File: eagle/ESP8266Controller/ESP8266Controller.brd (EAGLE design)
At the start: 61 x 48.3 mm, 22 parts, among them J1 POWER_JACKPTH

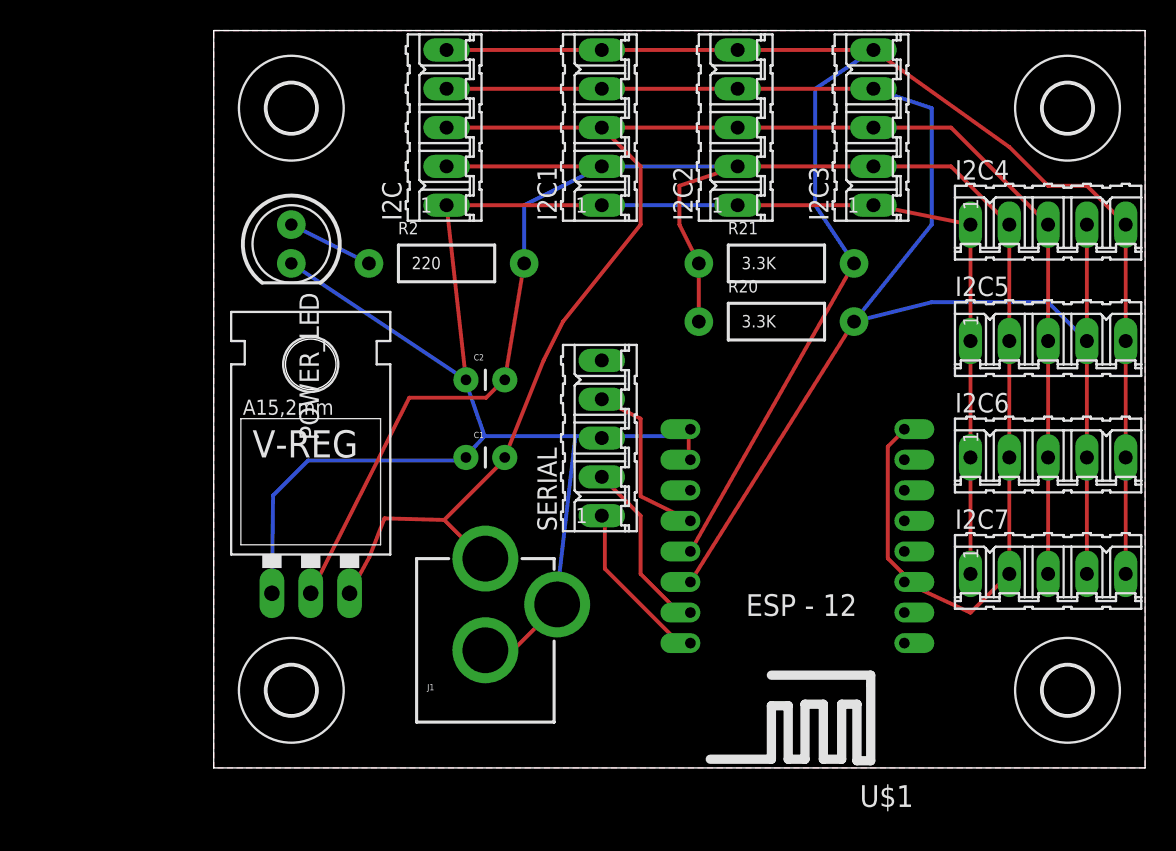
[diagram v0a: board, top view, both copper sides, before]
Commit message: 1.  More additions to the API 2.  Rename device.moduleIndex to device.port 3.  Begin work on new InputModule 4.  Module:  remove unused functions: 	virtual byte getDeviceCount(void) const = 0; 	virtual short getDeviceID(byte index) const = 0;
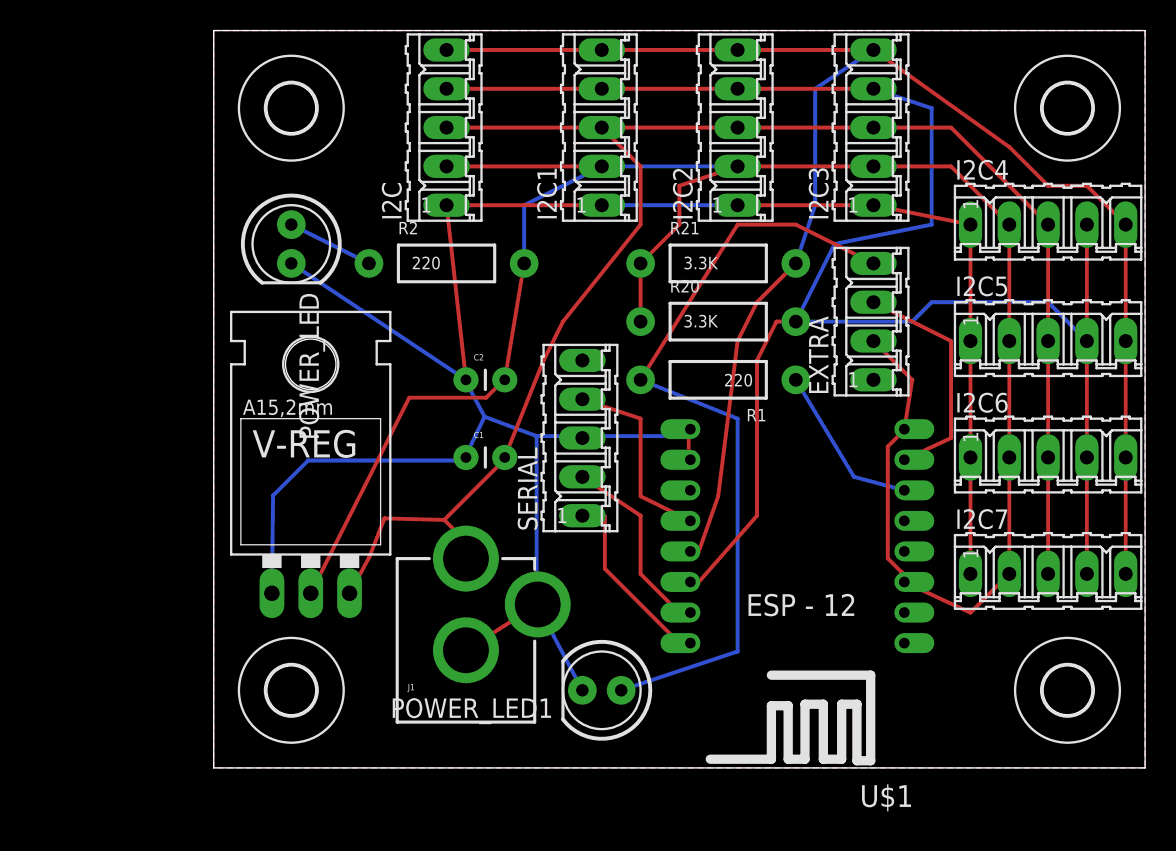
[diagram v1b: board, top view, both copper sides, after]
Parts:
- added EXTRA: PIN0, con-amp-quick:04P
- added POWER_LED1: 3.3, SparkFun-LED:LED5MM
- added R1: 220, SparkFun-Resistors:AXIAL-0.4
- moved R20 3.81 mm to (33.0, 29.2)
- moved R21 3.81 mm to (33.0, 33.0)
- moved J1 1.27 mm to (16.5, 0.00)
- moved SERIAL 1.27 mm to (24.1, 21.6)
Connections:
- removed net N$34: U$1.GPIO14
- removed net N$35: U$1.GPIO12
- removed net N$36: U$1.GPIO2
- new net N$1: EXTRA.4, POWER_LED1.A, R1.P$2
- new net N$2: R1.P$1, U$1.GPIO12
- new net N$3: EXTRA.3, U$1.GPIO13
- net +3V3: now also EXTRA.2
- net GND: now also EXTRA.1, POWER_LED1.K
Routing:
- net N$1: track 0.00 -> 51.6 mm
- net N$3: track 0.00 -> 15.4 mm
- net N$2: track 0.00 -> 10.8 mm
- net N$8: track 107.1 -> 115.8 mm
- net +3V3: track 132.0 -> 139.6 mm
- net GND: track 141.5 -> 147.4 mm
- net N$4: track 11.2 -> 12.5 mm
- net N$6: track 109.9 -> 108.7 mm
- net N$19: track 11.6 -> 12.7 mm
- net N$11: track 11.7 -> 12.7 mm
- net VCC: track 108.9 -> 109.8 mm

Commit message: 1.  Cleanup continues.  BlockController and the corresponding controller are deprecated along with SignalController and it's controller board.  These are replaced by the InputModule and OutputModule respectively 2.  TurnoutHandler moved to the MultiModuleController project folder 3.  Module moved to the MultiModuleController project folder 4.  More database cleanup work completed.
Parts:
- removed POWER_LED1: 3.3, SparkFun-LED:LED5MM
- EXTRA: value PIN0 -> (none)
- I2C, I2C1, I2C2, I2C3, I2C4, I2C5, I2C6, I2C7: value PIN1 -> (none)
- turned R1 to 0 degrees
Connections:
- net N$6 renamed SDA
- net N$8 renamed SCL
- net GND: no longer POWER_LED1.K
- net N$1: no longer POWER_LED1.A
- net N$2: now also U$1.GPIO2; no longer U$1.GPIO12
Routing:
- net N$1: track 51.6 -> 10.2 mm
- net VCC: track 109.8 -> 106.9 mm
- net N$2: track 10.8 -> 9.73 mm
- net N$19: track 12.7 -> 12.0 mm
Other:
- board text added: "+"
- board text added: "-"
- board text added: "Layout Ctrl ESP 8266 Controller Version 2.1"
- board text added: "PIN0"
- board text added: "PWR"

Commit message: 1.  Add jitter-detection to BlockDevice 2.  Add flashing pins to  ModuleData 3.  Move flashing pin code from PanelOutputDevice to OutputModule.  This insures pins blink at the same rate and same state. 4.  Fix flashing code for PanelInputDevice/OutputModule 5.  Remove unused code from PanelInputDevice 6.  fix jitter-detection code in TurnoutDevice 7.  New checkbox on StatusDialog allows enabling/disabling of server heartbeat messages 8.  Remove one of the I2C connections from the LCS Controller to make room for labels for the I2C pins 9.  Up build version to 19
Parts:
- removed I2C7: (no value), con-amp-quick:05P
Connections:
- net +3V3: no longer I2C7.2
- net GND: no longer I2C7.1
- net SCL: no longer I2C7.4
- net SDA: no longer I2C7.5
- net VCC: no longer I2C7.3
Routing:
- net VCC: track 106.9 -> 99.3 mm
- net SDA: track 108.7 -> 101.1 mm
- net SCL: track 115.8 -> 108.2 mm
- net GND: track 147.9 -> 140.3 mm
- net +3V3: track 139.6 -> 134.5 mm
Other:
- board text added: "+3.3v"
- board text added: ".1uF"
- board text added: "10uF"
- board text added: "GND"
- board text added: "LCS Controller Version 2.2"
- board text added: "SCA"
- board text added: "SCL"
- board text added: "VCC"
- board text removed: "Layout Ctrl ESP 8266 Controller Version 2.1"
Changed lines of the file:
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@@
 <wire x1="60.96" y1="48.26" x2="0" y2="48.26" width="0" layer="20"/>
 <wire x1="0" y1="48.26" x2="0" y2="0" width="0" layer="20"/>
-<text x="29.21" y="1.27" size="1.27" layer="21" rot="R90">Layout Ctrl
-ESP 8266
+<text x="27.94" y="1.27" size="1.27" layer="21" rot="R90">LCS
 Controller
-Version 2.1</text>
+Version 2.2</text>
 <text x="46.99" y="24.13" size="1.27" layer="21" rot="R90">PIN0</text>
 <text x="6.35" y="38.1" size="1.778" layer="21" rot="R315">PWR</text>
@@
 <text x="19.05" y="17.78" size="1.778" layer="21">+</text>
 <text x="20.32" y="35.56" size="1.778" layer="21" rot="R90">PIN0</text>
-<text x="48.26" y="15.24" size="1.778" layer="21">PIN0</text>
+<text x="49.53" y="13.97" size="1.27" layer="21" rot="R90">GND</text>
+<text x="52.07" y="12.7" size="1.27" layer="21" rot="R90">+3.3v</text>
+<text x="54.61" y="13.97" size="1.27" layer="21" rot="R90">VCC</text>
+<text x="57.15" y="13.97" size="1.27" layer="21" rot="R90">SCL</text>
+<text x="59.69" y="13.97" size="1.27" layer="21" rot="R90">SCA</text>
+<text x="19.05" y="29.21" size="1.27" layer="21" rot="R180">10uF</text>
+<text x="19.05" y="19.05" size="1.27" layer="21" rot="R180">.1uF</text>
 </plain>
 <attributes>
@@
 <attribute name="OC_FARNELL" value="unknown" x="54.61" y="20.32" size="1.778" layer="27" display="off"/>
 </element>
-<element name="I2C7" library="con-amp-quick" package="05P" value="" x="54.61" y="12.7">
-<attribute name="OC_NEWARK" value="unknown" x="54.61" y="12.7" size="1.778" layer="27" display="off"/>
-<attribute name="MPN" value="" x="54.61" y="12.7" size="1.778" layer="27" display="off"/>
-<attribute name="MF" value="" x="54.61" y="12.7" size="1.778" layer="27" display="off"/>
-<attribute name="OC_FARNELL" value="unknown" x="54.61" y="12.7" size="1.778" layer="27" display="off"/>
-</element>
 <element name="R1" library="SparkFun-Resistors" package="AXIAL-0.4" value="220" x="33.02" y="25.4"/>
 <element name="EXTRA" library="con-amp-quick" package="04P" value="" x="43.18" y="29.21" rot="R90">
@@
 <contactref element="I2C5" pad="1"/>
 <contactref element="I2C6" pad="1"/>
-<contactref element="I2C7" pad="1"/>
 <wire x1="5.08" y1="33.02" x2="16.51" y2="25.4" width="0.254" layer="16"/>
 <wire x1="15.24" y1="36.83" x2="25.4" y2="36.83" width="0.254" layer="1"/>
@@
 </polygon>
 <wire x1="49.53" y1="20.32" x2="49.53" y2="27.94" width="0.254" layer="1"/>
-<wire x1="49.53" y1="12.7" x2="49.53" y2="20.32" width="0.254" layer="1"/>
 <wire x1="49.53" y1="27.94" x2="49.53" y2="35.56" width="0.254" layer="1"/>
 <wire x1="43.18" y1="36.83" x2="49.53" y2="35.56" width="0.254" layer="1"/>
@@
 <wire x1="18.9738" y1="25.3746" x2="17.8308" y2="24.2316" width="0.254" layer="1"/>
 <wire x1="18.9738" y1="25.3746" x2="19.05" y2="25.4" width="0.254" layer="1"/>
-<wire x1="45.0342" y1="12.8016" x2="45.0342" y2="12.3444" width="0.254" layer="1"/>
-<wire x1="44.1198" y1="13.716" x2="45.0342" y2="12.8016" width="0.254" layer="1"/>
-<wire x1="44.1198" y1="21.0312" x2="44.1198" y2="13.716" width="0.254" layer="1"/>
-<wire x1="45.0342" y1="21.9456" x2="44.1198" y2="21.0312" width="0.254" layer="1"/>
-<wire x1="45.0342" y1="12.3444" x2="45.2" y2="12.17" width="0.254" layer="1"/>
-<wire x1="45.0342" y1="21.9456" x2="45.2" y2="22.17" width="0.254" layer="1"/>
 <contactref element="I2C1" pad="2"/>
 <contactref element="I2C2" pad="2"/>
@@
 <contactref element="I2C5" pad="2"/>
 <contactref element="I2C6" pad="2"/>
-<contactref element="I2C7" pad="2"/>
 <wire x1="34.29" y1="39.37" x2="43.18" y2="39.37" width="0.254" layer="1"/>
 <wire x1="25.4" y1="39.37" x2="15.24" y2="39.37" width="0.254" layer="1"/>
 <wire x1="19.05" y1="25.4" x2="20.32" y2="33.02" width="0.254" layer="1"/>
-<wire x1="45.2" y1="12.17" x2="49.53" y2="10.16" width="0.254" layer="1"/>
-<wire x1="49.53" y1="10.16" x2="52.07" y2="12.7" width="0.254" layer="1"/>
 <wire x1="52.07" y1="20.32" x2="52.07" y2="27.94" width="0.254" layer="1"/>
-<wire x1="52.07" y1="12.7" x2="52.07" y2="20.32" width="0.254" layer="1"/>
 <wire x1="52.07" y1="27.94" x2="52.07" y2="35.56" width="0.254" layer="1"/>
 <wire x1="43.18" y1="39.37" x2="48.26" y2="39.37" width="0.254" layer="1"/>
@@
 <wire x1="43.18" y1="27.94" x2="45.72" y2="25.4" width="0.254" layer="1"/>
 <wire x1="45.72" y1="25.4" x2="45.2" y2="22.17" width="0.254" layer="1"/>
+<wire x1="45.2" y1="22.17" x2="43.18" y2="20.32" width="0.254" layer="1"/>
+<wire x1="43.18" y1="20.32" x2="43.18" y2="12.7" width="0.254" layer="1"/>
+<wire x1="43.18" y1="12.7" x2="45.2" y2="12.17" width="0.254" layer="1"/>
+<wire x1="52.07" y1="27.94" x2="50.8" y2="25.4" width="0.254" layer="16"/>
+<wire x1="50.8" y1="25.4" x2="45.2" y2="22.17" width="0.254" layer="16"/>
 </signal>
 <signal name="VCC">
@@
 <contactref element="I2C5" pad="3"/>
 <contactref element="I2C6" pad="3"/>
-<contactref element="I2C7" pad="3"/>
 <wire x1="43.18" y1="41.91" x2="34.29" y2="41.91" width="0.254" layer="1"/>
 <wire x1="34.29" y1="41.91" x2="25.4" y2="41.91" width="0.254" layer="1"/>
@@
 <wire x1="27.94" y1="39.37" x2="25.4" y2="41.91" width="0.254" layer="1"/>
 <wire x1="54.61" y1="20.32" x2="54.61" y2="27.94" width="0.254" layer="1"/>
-<wire x1="54.61" y1="12.7" x2="54.61" y2="20.32" width="0.254" layer="1"/>
 <wire x1="54.61" y1="27.94" x2="54.61" y2="35.56" width="0.254" layer="1"/>
 <wire x1="43.18" y1="41.91" x2="48.26" y2="41.91" width="0.254" layer="1"/>
@@
 <contactref element="I2C5" pad="5"/>
 <contactref element="I2C6" pad="5"/>
-<contactref element="I2C7" pad="5"/>
-<wire x1="59.69" y1="12.7" x2="59.69" y2="20.32" width="0.254" layer="1"/>
 <wire x1="43.18" y1="46.99" x2="34.29" y2="46.99" width="0.254" layer="1"/>
 <wire x1="34.29" y1="46.99" x2="25.4" y2="46.99" width="0.254" layer="1"/>
@@
 <contactref element="I2C5" pad="4"/>
 <contactref element="I2C6" pad="4"/>
-<contactref element="I2C7" pad="4"/>
 <wire x1="15.24" y1="44.45" x2="25.4" y2="44.45" width="0.254" layer="1"/>
 <wire x1="25.4" y1="44.45" x2="34.29" y2="44.45" width="0.254" layer="1"/>
@@
 <wire x1="40.64" y1="34.29" x2="38.1" y2="29.21" width="0.254" layer="16"/>
 <wire x1="57.15" y1="20.32" x2="57.15" y2="27.94" width="0.254" layer="1"/>
-<wire x1="57.15" y1="12.7" x2="57.15" y2="20.32" width="0.254" layer="1"/>
 </signal>
 <signal name="N$2">

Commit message: 1.  Add copyDevice to API 2.  Add modelChanged property to JSonModel
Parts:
- SERIAL: value PIN1 -> PIN0
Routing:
- added copper zone on layer 16, net N$5
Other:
- board text added: "SDA"
- board text removed: "SCA"
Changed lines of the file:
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@@
 <text x="54.61" y="13.97" size="1.27" layer="21" rot="R90">VCC</text>
 <text x="57.15" y="13.97" size="1.27" layer="21" rot="R90">SCL</text>
-<text x="59.69" y="13.97" size="1.27" layer="21" rot="R90">SCA</text>
+<text x="59.69" y="13.97" size="1.27" layer="21" rot="R90">SDA</text>
 <text x="19.05" y="29.21" size="1.27" layer="21" rot="R180">10uF</text>
 <text x="19.05" y="19.05" size="1.27" layer="21" rot="R180">.1uF</text>
@@
 <element name="R20" library="SparkFun-Resistors" package="AXIAL-0.4" value="3.3K" x="33.02" y="29.21"/>
 <element name="R21" library="SparkFun-Resistors" package="AXIAL-0.4" value="3.3K" x="33.02" y="33.02"/>
-<element name="SERIAL" library="con-amp-quick" package="05P" value="PIN1" x="24.13" y="21.59" rot="R90">
+<element name="SERIAL" library="con-amp-quick" package="05P" value="PIN0" x="24.13" y="21.59" rot="R90">
 <attribute name="MPN" value="" x="24.13" y="21.59" size="1.778" layer="27" rot="R90" display="off"/>
 <attribute name="MF" value="" x="24.13" y="21.59" size="1.778" layer="27" rot="R90" display="off"/>
@@
 <wire x1="40.64" y1="31.75" x2="43.18" y2="33.02" width="0.254" layer="1"/>
 </signal>
+<signal name="N$5">
+<polygon width="0.254" layer="16" isolate="0.3048">
+<vertex x="0" y="0"/>
+<vertex x="0" y="48.26"/>
+<vertex x="60.96" y="48.26"/>
+<vertex x="60.96" y="0"/>
+</polygon>
+</signal>
 </signals>

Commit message: New Update!
1.  Documentation checked in
2.  Two new messages:  SYS_DEVICE_CONFIG_CHANGED and SYS_ROUTE_CONFIG_CHANGED are now sent out by the API whenever a route or a device's configuration is changed.  The controllers respond by downloading the updated route or the updated device configuration.  In the case of a device configuration change, the controller also downloads it's notification list just in case it has changed as well.
3.  TurnoutDetails.qml now has the DeviceProperties section displayed
4.  PanelOutputDevice now supports multiple routes.  When ONVALUE is set to 1, the LED remains ON if ANY of the routes are active.  When ONVALUE is set to 0, the LED is ON only if ALL routes are in-active.
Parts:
- added X1: 14867, con-4ucon:14867
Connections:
- net GND: now also X1.1
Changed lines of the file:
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@@
 <attribute name="OC_FARNELL" value="unknown" x="43.18" y="29.21" size="1.778" layer="27" rot="R90" display="off"/>
+</element>
+<element name="X1" library="con-4ucon" package="14867" value="14867" x="-6.35" y="7.62">
+<attribute name="MPN" value="" x="-6.35" y="7.62" size="1.778" layer="27" display="off"/>
+<attribute name="MF" value="" x="-6.35" y="7.62" size="1.778" layer="27" display="off"/>
+<attribute name="OC_FARNELL" value="unknown" x="-6.35" y="7.62" size="1.778" layer="27" display="off"/>
+<attribute name="OC_NEWARK" value="unknown" x="-6.35" y="7.62" size="1.778" layer="27" display="off"/>
 </element>
 </elements>
@@
 <wire x1="16.51" y1="7.7" x2="21.21" y2="10.7" width="0.254" layer="1"/>
 <wire x1="43.18" y1="25.4" x2="49.53" y2="27.94" width="0.254" layer="16"/>
+<contactref element="X1" pad="1"/>
+<wire x1="-8.255" y1="13.97" x2="3.81" y2="11.43" width="0" layer="19" extent="1-1"/>
 </signal>
 <signal name="N$7">
